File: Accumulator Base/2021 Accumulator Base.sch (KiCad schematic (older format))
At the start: 38 parts, among them J1 J, J10 AIR+ LV, J11 Conn_01x13, J16 Reset button, J17 Inverter-, J2 BMB, J3 TSMPs, J4 Inv&Bat+, J5 Conn_01x10, J7 Conn_01x08, J8 Conn_01x12, J9 AIR+ LV, Q3 Q_NMOS_DGS, Q4 Q_NMOS_DGS, Q5 Q_NMOS_DGS, Q6 Q_NMOS_DGS, Q7 Q_NMOS_DGS, Q9 Q_NMOS_DGS, U1 74HC86, U2 IMD, U3 SDC-CUFR-Full-Library, U5 PWR_Transducer, U8 AIL&TSAL

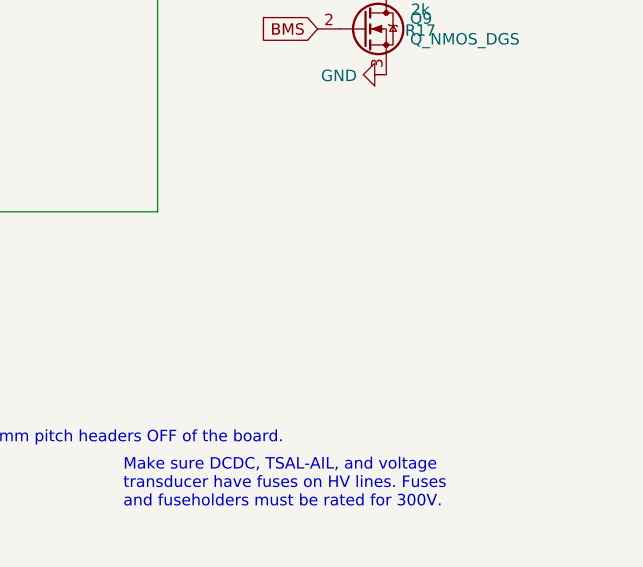
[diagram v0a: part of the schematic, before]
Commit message: Energy meter LV power connector added to Accumulator Base schematic
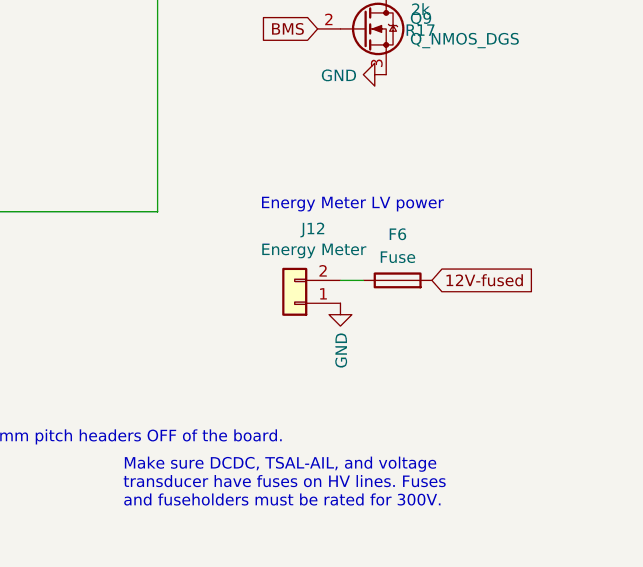
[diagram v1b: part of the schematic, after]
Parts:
- added F6: Fuse, symbol Device:Fuse
- added J12: Energy Meter, symbol Connector_Generic:Conn_01x02
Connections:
- net 12V-fused: now also F6.2
- net GND: now also J12.1 (Pin_1)
- new net: F6.1, J12.2 (Pin_2)
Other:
- note added: "Energy Meter LV power"
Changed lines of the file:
@@
 Text Notes 2050 2250 0    50   ~ 0
 Reset option for "testing" only
+$Comp
+L Connector_Generic:Conn_01x02 J12
+U 1 1 5F16BD14
+P 9800 6100
+F 0 "J12" H 9718 5775 50  0000 C CNN
+F 1 "Energy Meter" H 9718 5866 50  0000 C CNN
+F 2 "" H 9800 6100 50  0001 C CNN
+F 3 "~" H 9800 6100 50  0001 C CNN
+	1    9800 6100
+	-1   0    0    1
+$EndComp
+$Comp
+L power:GND #PWR?
+U 1 1 5F16C94A
+P 10000 6100
+AR Path="/5E8356A3/5F16C94A" Ref="#PWR?"  Part="1"
+AR Path="/5F16C94A" Ref="#PWR0103"  Part="1"
+F 0 "#PWR0103" H 10000 5850 50  0001 C CNN
+F 1 "GND" V 10005 5972 50  0000 R CNN
+F 2 "" H 10000 6100 50  0001 C CNN
+F 3 "" H 10000 6100 50  0001 C CNN
+	1    10000 6100
+	1    0    0    -1
+$EndComp
+$Comp
+L Device:Fuse F6
+U 1 1 5F16D16E
+P 10250 6000
+F 0 "F6" V 10450 6000 50  0000 C CNN
+F 1 "Fuse" V 10350 6000 50  0000 C CNN
+F 2 "" V 10180 6000 50  0001 C CNN
+F 3 "~" H 10250 6000 50  0001 C CNN
+	1    10250 6000
+	0    -1   -1   0
+$EndComp
+Text GLabel 10400 6000 2    50   Input ~ 0
+12V-fused
+Wire Wire Line
+	10100 6000 10000 6000
+Text Notes 9650 5700 0    50   ~ 0
+Energy Meter LV power
 $EndSCHEMATC

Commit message: Accumulator Base layout with no traces
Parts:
- removed J1: J, Connector_PinHeader_2.54mm:PinHeader_1x02_P2.54mm_Vertical, symbol Connector_Generic:Conn_01x02
- removed J10, J9: AIR+ LV, Connector_PinHeader_2.54mm:PinHeader_1x04_P2.54mm_Vertical, symbol Connector_Generic:Conn_01x04
- removed J11: Conn_01x13, symbol Connector_Generic:Conn_01x13
- removed Q5, Q7, Q9: Q_NMOS_DGS, Package_TO_SOT_THT:TO-220-3_Horizontal_TabDown, symbol Device:Q_NMOS_DGS
- removed R15, R17: 2k, symbol Device:R
- removed unit 3 of U1
- removed unit 4 of U1
- added C10, C11, C12, C13, C14, C6, C8: 100n, Capacitor_SMD:C_0805_2012Metric, symbol pspice:C
- added C7, C9: 10n, Capacitor_SMD:C_0805_2012Metric, symbol pspice:C
- added J10: Inverter&Motor, Connector_Molex:Molex_Mini-Fit_Jr_5566-10A_2x05_P4.20mm_Vertical, symbol Connector_Generic:Conn_01x10
- added J11, J14, J15: Jumper, Connector_PinHeader_2.54mm:PinHeader_1x02_P2.54mm_Vertical, symbol Connector_Generic:Conn_01x02
- added J13: Dash, Connector_Molex:Molex_Mini-Fit_Jr_5569-12A2_2x06_P4.20mm_Horizontal, symbol Connector_Generic:Conn_01x12
- added J9: AIRs, Connector_Molex:Molex_Mini-Fit_Jr_5566-08A_2x04_P4.20mm_Vertical, symbol Connector_Generic:Conn_01x08
- added Q7, Q8: Q_NMOS_GDS, Package_TO_SOT_SMD:TO-252-2, symbol Device:Q_NMOS_GDS
- added R16: 120, Resistor_SMD:R_1206_3216Metric, symbol Device:R
- added R30, R31: R_US, Resistor_THT:R_Axial_DIN0617_L17.0mm_D6.0mm_P20.32mm_Horizontal, symbol Device:R_US
- F1, F2, F5: footprint (none) -> Fuse:Fuseholder_Cylinder-5x20mm_Schurter_0031_8201_Horizontal_Open
- F6: footprint (none) -> Fuse:Fuseholder_Blade_Mini_Keystone_3568
- J12: footprint (none) -> Connector_Molex:Molex_Micro-Fit_3.0_43650-0215_1x02_P3.00mm_Vertical
- J16: footprint Connector_PinHeader_2.54mm:PinHeader_1x02_P2.54mm_Vertical -> Connector_Molex:Molex_Micro-Fit_3.0_43650-0215_1x02_P3.00mm_Vertical
- J17: footprint (none) -> Connector_TE-Connectivity:TE_MATE-N-LOK_1-794374-x_1x01_P4.14mm_Horizontal
- J2: footprint Connector_PinHeader_2.54mm:PinHeader_1x06_P2.54mm_Vertical -> Connector_Molex:Molex_Mini-Fit_Jr_5566-06A_2x03_P4.20mm_Vertical
- J3: value TSMPs -> TSMP; footprint (none) -> Connector_Molex:Molex_Micro-Fit_3.0_43650-0315_1x03_P3.00mm_Vertical; symbol Connector_Generic:Conn_01x02 -> Connector_Generic:Conn_01x03
- J4: footprint (none) -> Connector_TE-Connectivity:TE_MATE-N-LOK_1-770966-x_1x02_P4.14mm_Horizontal
- J5: value Conn_01x10 -> Peripherals; footprint (none) -> Connector_Molex:Molex_Mini-Fit_Jr_5569-18A2_2x09_P4.20mm_Horizontal; symbol Connector_Generic:Conn_01x10 -> Connector_Generic:Conn_01x18
- J7: value Conn_01x08 -> Interlocks; footprint (none) -> Connector_Molex:Molex_Mini-Fit_Jr_5566-08A_2x04_P4.20mm_Vertical
- J8: value Conn_01x12 -> Main LV; footprint (none) -> Connector_Molex:Molex_Mini-Fit_Jr_5569-10A2_2x05_P4.20mm_Horizontal; symbol Connector_Generic:Conn_01x12 -> Connector_Generic:Conn_01x10
- Q3, Q4, Q6: value Q_NMOS_DGS -> Q_NMOS_GDS; footprint Package_TO_SOT_THT:TO-220-3_Horizontal_TabDown -> Package_TO_SOT_SMD:TO-252-2; symbol Device:Q_NMOS_DGS -> Device:Q_NMOS_GDS
- R1, R10, R11, R12, R14, R2, R7, R8: footprint (none) -> Resistor_SMD:R_1206_3216Metric
- R13: value 2k -> 10k; footprint (none) -> Resistor_SMD:R_1206_3216Metric
- R9: value 2k2 -> 10k; footprint (none) -> Resistor_SMD:R_1206_3216Metric
- U1: footprint (none) -> CUFR-Full-Footprint-Library:74HC86DR2G
- U3: symbol EV2021_schematic-rescue:SDC-CUFR-Full-Library -> CUFR-Full-Library:SDC
- U5: footprint (none) -> Power_Transducer:PWR_Transducer
- U8: footprint (none) -> AIL&TSAL:AIL&TSAL
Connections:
- net GLV_12V is gone; now on net 5V-fused: J8.1 (Pin_1)
- net 12V-fused: now also J5.18 (Pin_18), J8.4 (Pin_4), Q3.2 (D), Q4.2 (D), C6.1, C7.1, Q8.2 (D); no longer Q3.1 (D), Q4.1 (D), R13.2
- net 5V-fused: now also C8.1, C9.1, Q7.2 (D)
- net BSPD: now also J13.8 (Pin_8); no longer J8.4 (Pin_4)
- net CAN-H: now also J5.16 (Pin_16), J8.6 (Pin_6), J10.3 (Pin_3), J11.1 (Pin_1), J13.9 (Pin_9); no longer J8.7 (Pin_7)
- net CAN-L: now also J5.17 (Pin_17), J8.7 (Pin_7), J10.4 (Pin_4), J13.10 (Pin_10), R16.1; no longer J8.8 (Pin_8)
- net DCDC_ON: now also J13.2 (Pin_2)
- net GND: now also J5.15 (Pin_15), J8.8 (Pin_8), J8.9 (Pin_9), R13.2, C10.1, C11.2, C12.2, C13.2, C14.2, C6.2, C7.2, C8.2, C9.2, J10.1 (Pin_1), J10.2 (Pin_2), J10.5 (Pin_5), J10.6 (Pin_6), J10.7 (Pin_7), J10.8 (Pin_8), J13.11 (Pin_11), J9.3 (Pin_3), J9.7 (Pin_7); no longer J8.11 (Pin_11), J8.12 (Pin_12)
- net SDC_open: now also Q6.2 (D), R31.2; no longer Q6.1 (D)
- net SDC_out: now also J5.11 (Pin_11); no longer J7.1 (Pin_1)
- net Safe_in: now also J8.5 (Pin_5), Q6.1 (G), C14.1, J9.4 (Pin_4); no longer J8.6 (Pin_6), Q6.2 (G)
- net Safe_out: now also J13.12 (Pin_12); no longer J8.5 (Pin_5)
- net TS_Ready: now also R30.2
- net sheet5F13132B/AIR+: now also J9.8 (Pin_8)
- net sheet5F13132C/BMS_Fault: now also Q4.1 (G), C13.1; no longer Q4.2 (G)
- net sheet5F13132C/Reset: now also Q3.1 (G), C12.1; no longer Q3.2 (G)
- net at R1.2: now also J3.3 (Pin_3); no longer J3.2 (Pin_2)
- net at U1.2: now also J9.5 (Pin_5)
- net at U1.1: now also J9.6 (Pin_6)
- net at U1.5: now also J9.1 (Pin_1)
- net at U1.4: now also J9.2 (Pin_2)
- net BMS: no longer names the net of Q4.3 (S), R11.1, U3.7 (BMS_Fault)
- net BSPD_F renamed RTD_ON
- net RTD_ON: now also J10.9 (Pin_9), Q8.3 (S)
- removed net Chassis: J8.9 (Pin_9), U2.3 (GND), U2.4 (GND)
- net HVD_InvInterlock renamed HVD_Charger
- net IMD renamed sheet5F13132C/IMD-output
- net sheet5F13132C/IMD-output: no longer R9.1
- net InvInterlock_TSMP renamed Charger_TSMP
- net TSMP_Charger renamed TSMP_Inv
- net sheet5F13132C/Current_Sens_High renamed Current_Sens_High
- net Current_Sens_High: now also J14.1 (Pin_1)
- net sheet5F13132C/Current_Sens_Low renamed Current_Sens_Low
- net Current_Sens_Low: now also J15.2 (Pin_2)
- new net: J11.2 (Pin_2), R16.2
- new net: J13.3 (Pin_3), R30.1
- new net: J13.7 (Pin_7), R31.1
- new net BMS_LED: J13.5 (Pin_5), U3.10 (BMS_LED)
- new net BSPD_LED: J13.4 (Pin_4), U3.9 (BSPD_LED)
- new net Chassis1: J5.13 (Pin_13), U2.3 (GND)
- new net Chassis2: J5.14 (Pin_14), U2.4 (GND)
- new net Current_Sens: J13.1 (Pin_1), J14.2 (Pin_2), J15.1 (Pin_1)
- new net HVD_HVD: J5.12 (Pin_12), J7.1 (Pin_1)
- new net IMD_LED: J13.6 (Pin_6), U3.8 (IMD_LED)
- new net RTD: C10.2, Q8.1 (G)
- new net Reg_EN: C11.1, Q7.1 (G)
- new net Reg_ON: J10.10 (Pin_10), Q7.3 (S), R9.1
- no-connect marks 7 -> 1
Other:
- note added: "Connect to TSMP\n"
- note added: "Inverter&Motor connections"
- note added: "Main LV Box connections"
- note removed: "Change IMD footprint, currently has 2.54mm pitch headers OFF of the board.\nWe want something on the board.\n"
- note removed: "Connect to TSMPs\n"
- note removed: "Jumpers for "testing" only"
- note removed: "LVMB connections"
- note removed: "Make sure DCDC, TSAL-AIL, and voltage \ntransducer have fuses on HV lines. Fuses \nand fuseholders must be rated for 300V."
- moved on the sheet: F6, J12, J16, J7, Q6, R11, R14, U1B, U1E

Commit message: Libraries added to project folders
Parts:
- removed R30: R_US, Resistor_THT:R_Axial_DIN0617_L17.0mm_D6.0mm_P20.32mm_Horizontal, symbol Device:R_US
- added J1, J18: Jumper, Connector_PinHeader_2.54mm:PinHeader_1x02_P2.54mm_Vertical, symbol Connector_Generic:Conn_01x02
- J10: value Inverter&Motor -> Inverter
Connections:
- net DCDC+: now also J5.3 (Pin_3); no longer J5.10 (Pin_10)
- net Green+: now also J5.10 (Pin_10); no longer J5.3 (Pin_3)
- net RTD_dash: now reaches J13.3 (Pin_3)
- net RTD_dash: now also J1.1 (Pin_1)
- net RTD renamed RTD_in
- net RTD_in: now also J1.2 (Pin_2), J18.1 (Pin_1)
- new net RTD_accu: J18.2 (Pin_2)
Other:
- note added: "Inverter connections"
- note removed: "Inverter&Motor connections"
- moved on the sheet: C10, C14, J11, Q6, Q8, R13, R14, R16

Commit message: Changed right angle connectors to straight ones and added LCD and EM connectors
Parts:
- added J19: EnergyMeter-IN, Connector_Molex:Molex_Micro-Fit_3.0_43650-0415_1x04_P3.00mm_Vertical, symbol Connector_Generic:Conn_01x04
- J10: value Inverter -> Inverter&Motor
- J12: value Energy Meter -> EnergyMeter-OUT; footprint Connector_Molex:Molex_Micro-Fit_3.0_43650-0215_1x02_P3.00mm_Vertical -> Connector_Molex:Molex_Micro-Fit_3.0_43650-0415_1x04_P3.00mm_Vertical; symbol Connector_Generic:Conn_01x02 -> Connector_Generic:Conn_01x04
- J13: footprint Connector_Molex:Molex_Mini-Fit_Jr_5569-12A2_2x06_P4.20mm_Horizontal -> Connector_Molex:Molex_Mini-Fit_Jr_5566-12A_2x06_P4.20mm_Vertical
- J17: footprint Connector_TE-Connectivity:TE_MATE-N-LOK_1-794374-x_1x01_P4.14mm_Horizontal -> Connector_Molex:Molex_Mini-Fit_Jr_5566-02A2_2x01_P4.20mm_Vertical; symbol Connector_Generic:Conn_01x01 -> Connector_Generic:Conn_01x02
- J4: footprint Connector_TE-Connectivity:TE_MATE-N-LOK_1-770966-x_1x02_P4.14mm_Horizontal -> Connector_Molex:Molex_Mini-Fit_Jr_5566-04A2_2x02_P4.20mm_Vertical; symbol Connector_Generic:Conn_01x02 -> Connector_Generic:Conn_01x04
- J5: footprint Connector_Molex:Molex_Mini-Fit_Jr_5569-18A2_2x09_P4.20mm_Horizontal -> Connector_Molex:Molex_Mini-Fit_Jr_5566-18A_2x09_P4.20mm_Vertical
- J8: footprint Connector_Molex:Molex_Mini-Fit_Jr_5569-10A2_2x05_P4.20mm_Horizontal -> Connector_Molex:Molex_Mini-Fit_Jr_5566-10A_2x05_P4.20mm_Vertical
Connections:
- net GND: now also J12.2 (Pin_2), J19.2 (Pin_2); no longer J12.1 (Pin_1)
- net inverter+: now also J4.1 (Pin_1)
- net inverter-: now also J17.2 (Pin_2)
- net sheet5F13132B/Battery+: now also J4.3 (Pin_3), J4.4 (Pin_4); no longer J4.1 (Pin_1)
- net at F6.1: now also J12.1 (Pin_1), J19.1 (Pin_1); no longer J12.2 (Pin_2)
- new net: J12.3 (Pin_3), J19.3 (Pin_3)
- new net: J12.4 (Pin_4), J19.4 (Pin_4)
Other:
- note added: "Inverter&Motor connections"
- note removed: "Inverter connections"
- moved on the sheet: F6
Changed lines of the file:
@@
 $EndComp
 $Comp
-L Connector_Generic:Conn_01x01 J?
+L Connector_Generic:Conn_01x02 J?
 U 1 1 5F271A92
 P 1550 4200
 AR Path="/5E8356A3/5F271A92" Ref="J?"  Part="1"
 AR Path="/5F271A92" Ref="J17"  Part="1"
-F 0 "J17" H 1468 3975 50  0000 C CNN
-F 1 "Inverter-" H 1468 4066 50  0000 C CNN
-F 2 "Connector_TE-Connectivity:TE_MATE-N-LOK_1-794374-x_1x01_P4.14mm_Horizontal" H 1550 4200 50  0001 C CNN
+F 0 "J17" H 1550 4000 50  0000 C CNN
+F 1 "Inverter-" H 1550 4300 50  0000 C CNN
+F 2 "Connector_Molex:Molex_Mini-Fit_Jr_5566-02A2_2x01_P4.20mm_Vertical" H 1550 4200 50  0001 C CNN
 F 3 "~" H 1550 4200 50  0001 C CNN
 	1    1550 4200
@@
 Connection ~ 2450 4500
 Wire Wire Line
-	2450 4500 2450 4550
-Wire Wire Line
 	5050 4000 5050 4500
 Wire Wire Line
@@
 Wire Wire Line
 	2550 4200 2550 4700
-Wire Wire Line
-	1750 4550 2450 4550
-Connection ~ 2450 4550
-Wire Wire Line
-	2450 4550 2450 5200
 $Comp
 L Device:Fuse F2
@@
 Text GLabel 3050 3950 0    50   Input ~ 0
 DCDC_ON
-Text Notes 7100 6350 0    118  ~ 0
+Text Notes 7100 7000 0    118  ~ 0
 Programming cable plugged in\nAdd external programming port connector\n
 Text GLabel 5100 1500 0    50   Input ~ 0
@@
 F 0 "J8" H 3300 1100 50  0000 L CNN
 F 1 "Main LV" H 3050 500 50  0000 L CNN
-F 2 "Connector_Molex:Molex_Mini-Fit_Jr_5569-10A2_2x05_P4.20mm_Horizontal" H 3200 1100 50  0001 C CNN
+F 2 "Connector_Molex:Molex_Mini-Fit_Jr_5566-10A_2x05_P4.20mm_Vertical" H 3200 1100 50  0001 C CNN
 F 3 "~" H 3200 1100 50  0001 C CNN
 	1    3200 1100
@@
 Safe_in
 $Comp
-L Connector_Generic:Conn_01x02 J4
+L Connector_Generic:Conn_01x04 J4
 U 1 1 5F3A574B
-P 1550 4650
-F 0 "J4" H 1468 4325 50  0000 C CNN
-F 1 "Inv&Bat+" H 1468 4416 50  0000 C CNN
-F 2 "Connector_TE-Connectivity:TE_MATE-N-LOK_1-770966-x_1x02_P4.14mm_Horizontal" H 1550 4650 50  0001 C CNN
-F 3 "~" H 1550 4650 50  0001 C CNN
-	1    1550 4650
+P 1550 4750
+F 0 "J4" H 1550 4450 50  0000 C CNN
+F 1 "Inv&Bat+" H 1550 4950 50  0000 C CNN
+F 2 "Connector_Molex:Molex_Mini-Fit_Jr_5566-04A2_2x02_P4.20mm_Vertical" H 1550 4750 50  0001 C CNN
+F 3 "~" H 1550 4750 50  0001 C CNN
+	1    1550 4750
 	-1   0    0    1
 $EndComp
@@
 Reset option for "testing" only
 $Comp
-L Connector_Generic:Conn_01x02 J12
+L Connector_Generic:Conn_01x04 J12
 U 1 1 5F16BD14
-P 10000 5750
-F 0 "J12" H 9918 5425 50  0000 C CNN
-F 1 "Energy Meter" H 9918 5516 50  0000 C CNN
-F 2 "Connector_Molex:Molex_Micro-Fit_3.0_43650-0215_1x02_P3.00mm_Vertical" H 10000 5750 50  0001 C CNN
-F 3 "~" H 10000 5750 50  0001 C CNN
-	1    10000 5750
+P 10100 6250
+F 0 "J12" H 10250 6150 50  0000 C CNN
+F 1 "EnergyMeter-OUT" H 10050 5900 50  0000 C CNN
+F 2 "Connector_Molex:Molex_Micro-Fit_3.0_43650-0415_1x04_P3.00mm_Vertical" H 10100 6250 50  0001 C CNN
+F 3 "~" H 10100 6250 50  0001 C CNN
+	1    10100 6250
 	-1   0    0    1
 $EndComp
@@
 L power:GND #PWR?
 U 1 1 5F16C94A
-P 10200 5750
+P 10400 6250
 AR Path="/5E8356A3/5F16C94A" Ref="#PWR?"  Part="1"
 AR Path="/5F16C94A" Ref="#PWR0103"  Part="1"
-F 0 "#PWR0103" H 10200 5500 50  0001 C CNN
-F 1 "GND" V 10205 5622 50  0000 R CNN
-F 2 "" H 10200 5750 50  0001 C CNN
-F 3 "" H 10200 5750 50  0001 C CNN
-	1    10200 5750
-	1    0    0    -1
+F 0 "#PWR0103" H 10400 6000 50  0001 C CNN
+F 1 "GND" V 10405 6122 50  0000 R CNN
+F 2 "" H 10400 6250 50  0001 C CNN
+F 3 "" H 10400 6250 50  0001 C CNN
+	1    10400 6250
+	0    -1   -1   0
 $EndComp
 $Comp
 L Device:Fuse F6
 U 1 1 5F16D16E
-P 10450 5650
-F 0 "F6" V 10650 5650 50  0000 C CNN
-F 1 "Fuse" V 10550 5650 50  0000 C CNN
-F 2 "Fuse:Fuseholder_Blade_Mini_Keystone_3568" V 10380 5650 50  0001 C CNN
-F 3 "~" H 10450 5650 50  0001 C CNN
-	1    10450 5650
+P 10550 6350
+F 0 "F6" V 10450 6500 50  0000 C CNN
+F 1 "Fuse" V 10450 6350 50  0000 C CNN
+F 2 "Fuse:Fuseholder_Blade_Mini_Keystone_3568" V 10480 6350 50  0001 C CNN
+F 3 "~" H 10550 6350 50  0001 C CNN
+	1    10550 6350
 	0    -1   -1   0
 $EndComp
-Text GLabel 10600 5650 2    50   Input ~ 0
+Text GLabel 10700 6350 2    50   Input ~ 0
 12V-fused
-Wire Wire Line
-	10300 5650 10200 5650
 Text Notes 9800 5350 0    50   ~ 0
 Energy Meter LV power
@@
 F 0 "J13" H 9600 600 50  0000 L CNN
 F 1 "Dash" H 9850 600 50  0000 L CNN
-F 2 "Connector_Molex:Molex_Mini-Fit_Jr_5569-12A2_2x06_P4.20mm_Horizontal" H 9950 1300 50  0001 C CNN
+F 2 "Connector_Molex:Molex_Mini-Fit_Jr_5566-12A_2x06_P4.20mm_Vertical" H 9950 1300 50  0001 C CNN
 F 3 "~" H 9950 1300 50  0001 C CNN
 	1    9950 1300
@@
 F 0 "J5" H 10600 600 50  0000 L CNN
 F 1 "Peripherals" H 10800 600 50  0000 L CNN
-F 2 "Connector_Molex:Molex_Mini-Fit_Jr_5569-18A2_2x09_P4.20mm_Horizontal" H 11100 1600 50  0001 C CNN
+F 2 "Connector_Molex:Molex_Mini-Fit_Jr_5566-18A_2x09_P4.20mm_Vertical" H 11100 1600 50  0001 C CNN
 F 3 "~" H 11100 1600 50  0001 C CNN
 	1    11100 1600
@@
 	0    1    1    0
 $EndComp
-Text Notes 1650 600  0    50   ~ 0
-Inverter connections
+Text Notes 1450 600  0    50   ~ 0
+Inverter&Motor connections
 $Comp
 L power:GND #PWR?
@@
 P 2300 1100
 F 0 "J10" H 2400 1100 50  0000 L CNN
-F 1 "Inverter" H 2150 500 50  0000 L CNN
+F 1 "Inverter&Motor" H 2050 500 50  0000 L CNN
 F 2 "Connector_Molex:Molex_Mini-Fit_Jr_5566-10A_2x05_P4.20mm_Vertical" H 2300 1100 50  0001 C CNN
 F 3 "~" H 2300 1100 50  0001 C CNN
@@
 P 9750 1800
 AR Path="/5E8356A3/5F3365A5" Ref="#PWR?"  Part="1"
-AR Path="/5F3365A5" Ref="#PWR?"  Part="1"
-F 0 "#PWR?" H 9750 1550 50  0001 C CNN
+AR Path="/5F3365A5" Ref="#PWR0116"  Part="1"
+F 0 "#PWR0116" H 9750 1550 50  0001 C CNN
 F 1 "GND" V 9755 1672 50  0000 R CNN
 F 2 "" H 9750 1800 50  0001 C CNN
@@
 P 2100 700
 AR Path="/5E8356A3/5F337CE2" Ref="#PWR?"  Part="1"
-AR Path="/5F337CE2" Ref="#PWR?"  Part="1"
-F 0 "#PWR?" H 2100 450 50  0001 C CNN
+AR Path="/5F337CE2" Ref="#PWR0125"  Part="1"
+F 0 "#PWR0125" H 2100 450 50  0001 C CNN
 F 1 "GND" V 2105 572 50  0000 R CNN
 F 2 "" H 2100 700 50  0001 C CNN
@@
 	0    1    1    0
 $EndComp
+$Comp
+L Connector_Generic:Conn_01x04 J19
+U 1 1 5F3641D1
+P 9450 6250
+F 0 "J19" H 9550 6150 50  0000 L CNN
+F 1 "EnergyMeter-IN" H 9150 5900 50  0000 L CNN
+F 2 "Connector_Molex:Molex_Micro-Fit_3.0_43650-0415_1x04_P3.00mm_Vertical" H 9450 6250 50  0001 C CNN
+F 3 "~" H 9450 6250 50  0001 C CNN
+	1    9450 6250
+	1    0    0    1
+$EndComp
+Wire Wire Line
+	10400 6350 10300 6350
+Wire Wire Line
+	9250 6050 10300 6050
+Wire Wire Line
+	10300 6150 9250 6150
+Wire Wire Line
+	10300 6250 9250 6250
+Wire Wire Line
+	9250 6350 10300 6350
+Connection ~ 10300 6350
+Wire Wire Line
+	10400 6250 10300 6250
+Connection ~ 10300 6250
+Wire Wire Line
+	1750 4100 1750 4200
+Connection ~ 1750 4200
+Wire Wire Line
+	2450 4500 2450 4850
+Wire Wire Line
+	1750 4850 2450 4850
+Connection ~ 2450 4850
+Wire Wire Line
+	2450 4850 2450 5200
+Wire Wire Line
+	1750 4750 1750 4850
+Connection ~ 1750 4850
+Wire Wire Line
+	1750 4550 1750 4650
+Connection ~ 1750 4650
 $EndSCHEMATC

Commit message: Replaced TSMP connector
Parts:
- J3: footprint Connector_Molex:Molex_Micro-Fit_3.0_43650-0315_1x03_P3.00mm_Vertical -> Connector_TE-Connectivity:TE_MATE-N-LOK_1-770870-x_1x03_P4.14mm_Vertical
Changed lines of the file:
@@
 F 0 "J3" H 1318 3075 50  0000 C CNN
 F 1 "TSMP" H 1318 3166 50  0000 C CNN
-F 2 "Connector_Molex:Molex_Micro-Fit_3.0_43650-0315_1x03_P3.00mm_Vertical" H 1400 3400 50  0001 C CNN
+F 2 "Connector_TE-Connectivity:TE_MATE-N-LOK_1-770870-x_1x03_P4.14mm_Vertical" H 1400 3400 50  0001 C CNN
 F 3 "~" H 1400 3400 50  0001 C CNN
 	1    1400 3400
